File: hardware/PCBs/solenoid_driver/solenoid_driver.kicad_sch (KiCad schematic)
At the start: 13 parts, among them J1 from_mainboard, J2 12V power, J3 to_solenoid2, J4 to_solenoid1, J5 12V power, Q1 Q_NMOS_GDS, Q2 Q_NMOS_GDS

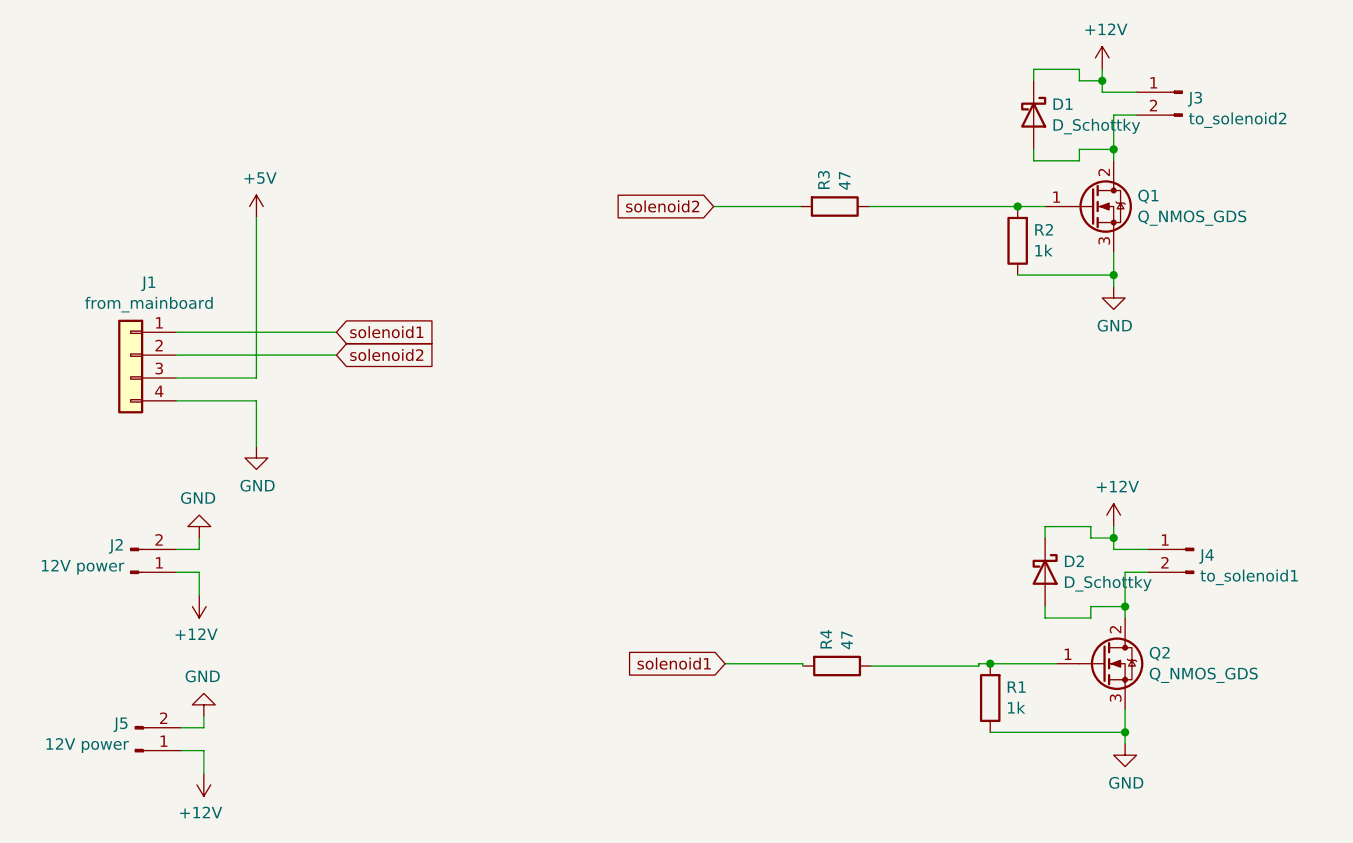
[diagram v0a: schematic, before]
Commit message: Update solenoid driver to v0.3
Update solenoid driver to v0.3:
- added driver IC and peripherals
- rearrangements in the board layout

Co-Authored-By: Andre Maia Chagas <a.maia-chagas@sussex.ac.uk>
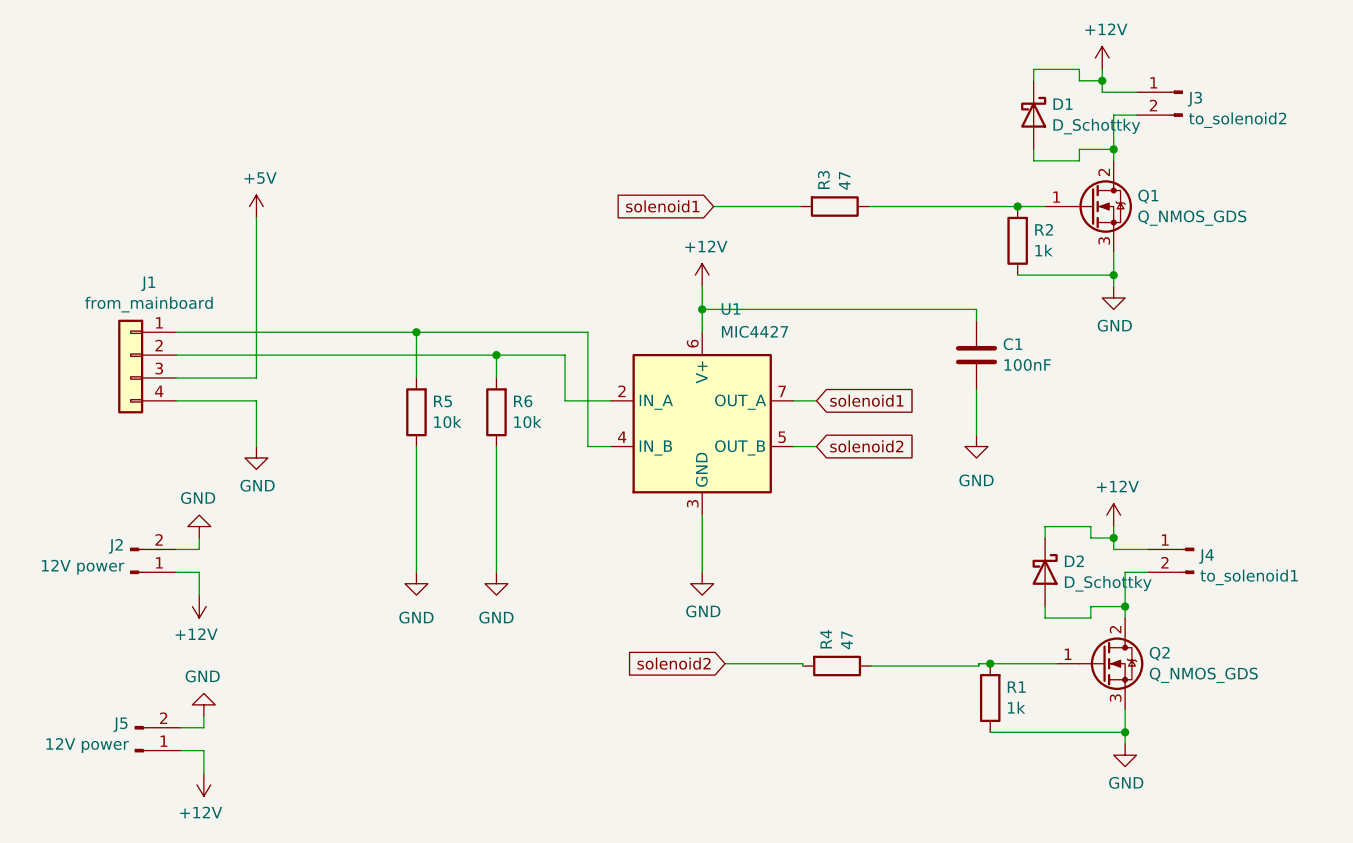
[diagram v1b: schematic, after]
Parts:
- added C1: 100nF, Capacitor_THT:C_Disc_D7.0mm_W2.5mm_P5.00mm, symbol Device:C
- added R5, R6: 10k, Resistor_THT:R_Box_L13.0mm_W4.0mm_P9.00mm, symbol Device:R
- added U1: MIC4427, Package_DIP:DIP-8_W7.62mm, symbol Driver_FET:MIC4427
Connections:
- net +12V: now also C1.1, U1.6 (V+)
- net GND: now also C1.2, R5.1, R6.1, U1.3 (GND)
- net solenoid1: now also R3.2, U1.7 (OUT_A); no longer J1.1 (Pin_1), R4.2
- net solenoid2: now also R4.2, U1.5 (OUT_B); no longer J1.2 (Pin_2), R3.2
- new net: J1.1 (Pin_1), R5.2, U1.4 (IN_B)
- new net: J1.2 (Pin_2), R6.2, U1.2 (IN_A)
